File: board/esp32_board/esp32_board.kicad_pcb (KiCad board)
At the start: 2 copper layers, 3 parts, among them J1 Screw_Terminal_01x19, J2 Screw_Terminal_01x19, U1 ESP32-DevKitC

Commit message: feat: Updated board
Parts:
- added J3: Conn_01x19_Socket, Connector_PinSocket_2.54mm:PinSocket_1x19_P2.54mm_Vertical, F.Cu at (118.5, 74.5)
- added J4: Conn_01x19_Pin, Connector_PinSocket_2.54mm:PinSocket_1x19_P2.54mm_Vertical, F.Cu at (100.5, 74.5)
- added J5: Conn_01x19_Socket, Connector_PinSocket_2.54mm:PinSocket_1x19_P2.54mm_Vertical, F.Cu at (180.0, 74.5)
- added J6: Conn_01x19_Pin, Connector_PinSocket_2.54mm:PinSocket_1x19_P2.54mm_Vertical, F.Cu at (199.0, 74.5)
- moved J1 27.5 mm to (218.5, 74.5)
- moved J2 23.0 mm to (80.5, 74.5)

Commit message: feat: Updated board and presentation
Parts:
- moved J1 122.3 mm to (108.0, 22.0)
- moved J6 113.8 mm to (98.0, 22.0)
- moved J5 105.9 mm to (88.0, 22.0)
- moved U1 98.9 mm to (51.5, 22.0)
- moved J3 92.8 mm to (42.0, 22.0)
- moved J4 86.3 mm to (32.0, 22.0)
- moved J2 78.6 mm to (22.0, 22.0)
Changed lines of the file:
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@@
 	(footprint "PCM_Espressif:ESP32-DevKitC"
 		(layer "F.Cu")
-		(at 135.215 74.54812)
+		(at 51.5 21.96)
 		(descr "ESP32-DevKitC: https://docs.espressif.com/projects/esp-idf/en/latest/esp32/hw-reference/esp32/get-started-devkitc.html")
 		(tags "ESP32")
@@
 	(footprint "Connector_PinSocket_2.54mm:PinSocket_1x19_P2.54mm_Vertical"
 		(layer "F.Cu")
-		(at 180 74.5)
+		(at 88 22)
 		(descr "Through hole straight socket strip, 1x19, 2.54mm pitch, single row (from Kicad 4.0.7), script generated")
 		(tags "Through hole socket strip THT 1x19 2.54mm single row")
@@
 	(footprint "Connector_PinHeader_2.54mm:PinHeader_1x19_P2.54mm_Vertical"
 		(layer "F.Cu")
-		(at 218.5 74.5)
+		(at 108 22)
 		(descr "Through hole straight pin header, 1x19, 2.54mm pitch, single row")
 		(tags "Through hole pin header THT 1x19 2.54mm single row")
@@
 	(footprint "Connector_PinSocket_2.54mm:PinSocket_1x19_P2.54mm_Vertical"
 		(layer "F.Cu")
-		(at 100.5 74.5)
+		(at 32 22)
 		(descr "Through hole straight socket strip, 1x19, 2.54mm pitch, single row (from Kicad 4.0.7), script generated")
 		(tags "Through hole socket strip THT 1x19 2.54mm single row")
@@
 	(footprint "Connector_PinSocket_2.54mm:PinSocket_1x19_P2.54mm_Vertical"
 		(layer "F.Cu")
-		(at 118.5 74.5)
+		(at 42 22)
 		(descr "Through hole straight socket strip, 1x19, 2.54mm pitch, single row (from Kicad 4.0.7), script generated")
 		(tags "Through hole socket strip THT 1x19 2.54mm single row")
@@
 	(footprint "Connector_PinHeader_2.54mm:PinHeader_1x19_P2.54mm_Vertical"
 		(layer "F.Cu")
-		(at 80.5 74.5)
+		(at 22 22)
 		(descr "Through hole straight pin header, 1x19, 2.54mm pitch, single row")
 		(tags "Through hole pin header THT 1x19 2.54mm single row")
@@
 	(footprint "Connector_PinSocket_2.54mm:PinSocket_1x19_P2.54mm_Vertical"
 		(layer "F.Cu")
-		(at 199 74.5)
+		(at 98 22)
 		(descr "Through hole straight socket strip, 1x19, 2.54mm pitch, single row (from Kicad 4.0.7), script generated")
 		(tags "Through hole socket strip THT 1x19 2.54mm single row")

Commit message: feat: Updated docs and board
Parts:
- added compass1: ~, slon_modules:compass, F.Cu at (108.5, 85.4)
- added gps1: ~, slon_modules:gps, F.Cu at (175.5, 88.3)
- added relay1: ~, slon_modules:relay, F.Cu at (147.5, 66.4)
- added relay2: ~, slon_modules:relay, F.Cu at (144.0, 70.4)
- moved J1 108.9 mm to (191.0, 92.5)
- moved J2 108.9 mm to (105.0, 92.5)
- moved J3 108.9 mm to (125.0, 92.5)
- moved J4 108.9 mm to (115.0, 92.5)
- moved J5 108.9 mm to (171.0, 92.5)
- moved J6 108.9 mm to (181.0, 92.5)
- moved U1 108.9 mm to (134.5, 92.4)

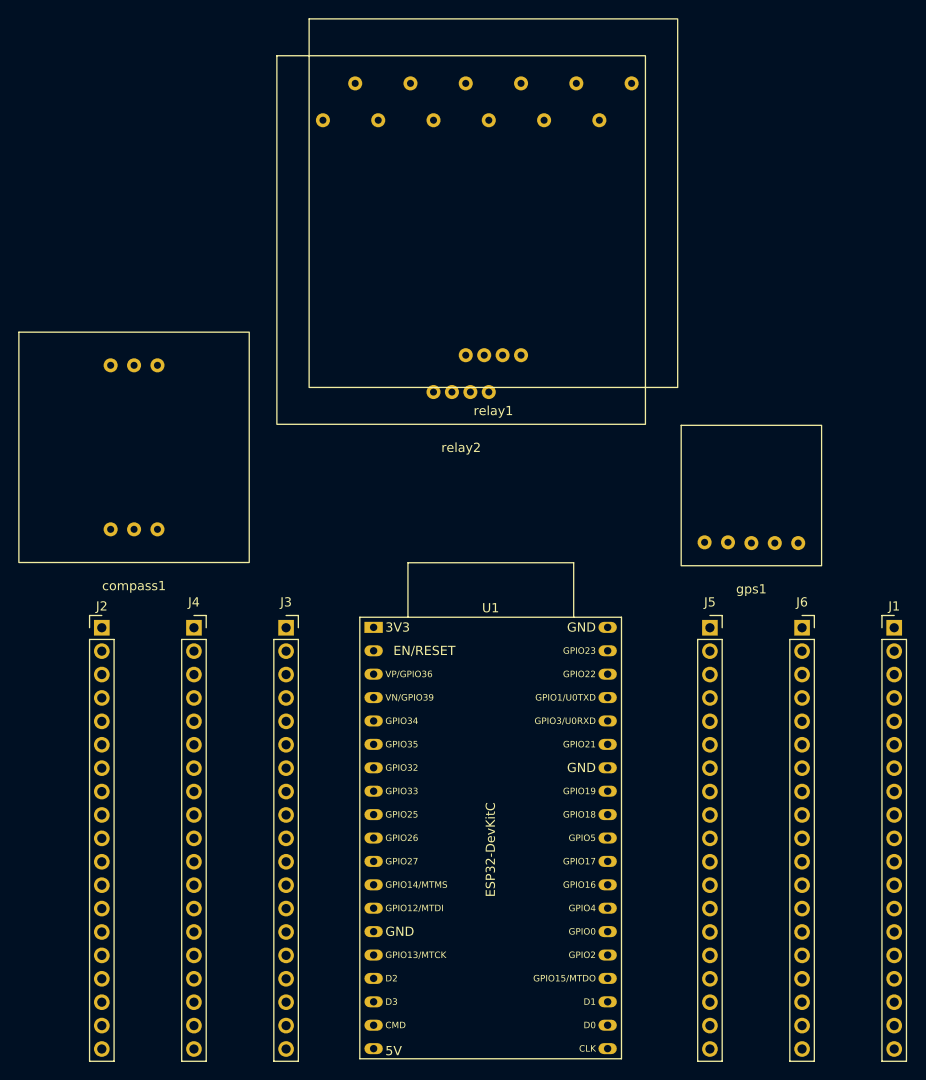
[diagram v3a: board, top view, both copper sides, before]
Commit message: feat(board): Added roads
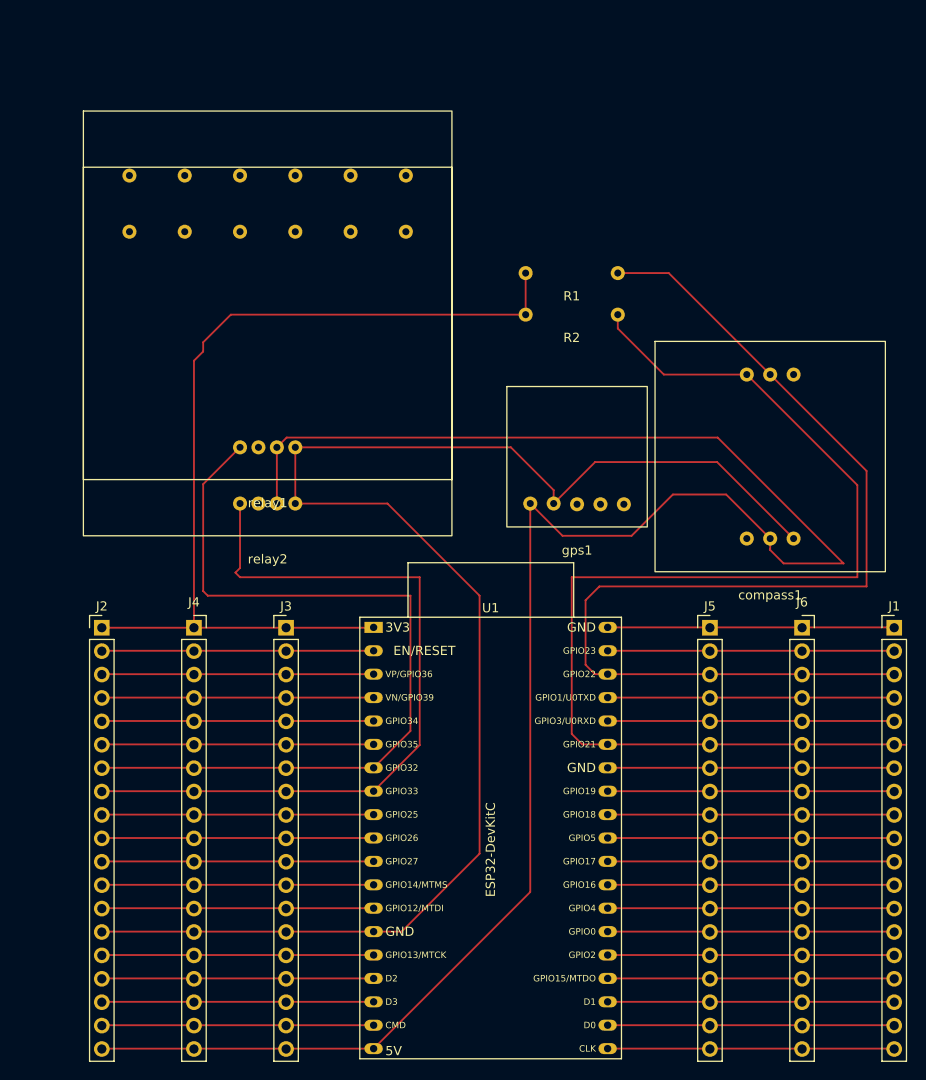
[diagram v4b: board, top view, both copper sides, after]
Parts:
- added R1: 2200, slon_modules:r, F.Cu at (156.0, 56.5)
- added R2: 2200, slon_modules:r, F.Cu at (156.0, 61.0)
- J3, J5: footprint Connector_PinSocket_2.54mm:PinSocket_1x19_P2.54mm_Vertical -> Connector_PinHeader_2.54mm:PinHeader_1x19_P2.54mm_Vertical
- moved compass1 69.0 mm to (177.5, 86.4)
- moved relay1 26.5 mm to (123.0, 76.4)
- moved relay2 24.2 mm to (123.0, 82.5)
- moved gps1 19.4 mm to (156.6, 84.1)
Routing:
- net GND: track 0.00 -> 227.8 mm
- net V5: track 0.00 -> 210.6 mm
- net 21: track 0.00 -> 129.4 mm
- net 22: track 0.00 -> 120.5 mm
- net 3V3: track 0.00 -> 101.7 mm
- net 32: track 0.00 -> 89.8 mm
- net 33: track 0.00 -> 82.7 mm
- net SD0: track 0.00 -> 31.1 mm
- net CLK: track 0.00 -> 31.1 mm
- net 15: track 0.00 -> 31.1 mm
- net RX: track 0.00 -> 31.1 mm
- net 5: track 0.00 -> 31.1 mm
- net 19: track 0.00 -> 31.1 mm
- net 16: track 0.00 -> 31.1 mm
- net 0: track 0.00 -> 31.1 mm
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
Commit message: feat(board): Updated board
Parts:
- moved relay1 0.10 mm to (123.0, 76.5)
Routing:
- net 16: track 31.1 -> 87.5 mm
- net V5: track 210.6 -> 158.0 mm
- net 17: track 31.1 -> 79.8 mm
- net GND: track 227.8 -> 214.2 mm
- net 3V3: track 101.7 -> 94.1 mm
- net 32: track 89.8 -> 85.7 mm
- net (no net): vias 0 -> 4
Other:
- board outline added: 95.5 x 106 mm

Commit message: feat(board): Updated board
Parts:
- removed relay1, relay2: ~, slon_modules:relay
- moved compass1 9.50 mm to (177.5, 76.9)
- moved gps1 3.50 mm to (153.1, 84.1)
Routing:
- net 32: track 85.7 -> 29.5 mm
- net 33: track 82.7 -> 29.5 mm
- net GND: track 214.2 -> 177.8 mm
- net V5: track 158.0 -> 179.3 mm
- net 3V3: track 94.1 -> 79.0 mm
- net 22: track 120.5 -> 134.7 mm
- net 21: track 129.4 -> 134.7 mm
- net 16: track 87.5 -> 91.4 mm
- net 17: track 79.8 -> 81.2 mm
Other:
- board size 95.5 x 106 mm -> 100 x 110 mm

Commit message: feat(board): Updated board
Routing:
- net 16: track 91.4 -> 86.8 mm
- net 17: track 81.2 -> 80.4 mm
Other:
- board size 100 x 110 mm -> 95.5 x 105 mm

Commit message: feat: Updated docs and board
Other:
- board size 95.5 x 105 mm -> 95.5 x 110 mm
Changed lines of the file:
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@@
 		(pad_to_mask_clearance 0)
 		(allow_soldermask_bridges_in_footprints no)
+		(grid_origin 100.25 35.5)
 		(pcbplotparams
-			(layerselection 0x00010fc_ffffffff)
+			(layerselection 0x0001000_7fffffff)
 			(plot_on_all_layers_selection 0x0000000_00000000)
 			(disableapertmacros no)
@@
 			(svgprecision 4)
 			(plotframeref no)
-			(viasonmask no)
+			(viasonmask yes)
 			(mode 1)
 			(useauxorigin no)
@@
 			(pdf_back_fp_property_popups yes)
 			(dxfpolygonmode yes)
-			(dxfimperialunits yes)
+			(dxfimperialunits no)
 			(dxfusepcbnewfont yes)
 			(psnegative no)
 			(psa4output no)
-			(plotreference yes)
-			(plotvalue yes)
-			(plotfptext yes)
+			(plotreference no)
+			(plotvalue no)
+			(plotfptext no)
 			(plotinvisibletext no)
 			(sketchpadsonfab no)
 			(subtractmaskfromsilk no)
-			(outputformat 1)
+			(outputformat 3)
 			(mirror no)
-			(drillshape 0)
+			(drillshape 2)
 			(scaleselection 1)
-			(outputdirectory "gbr/")
+			(outputdirectory "dxf/")
 		)
 	)
@@
 	)
 	(gr_rect
-		(start 100 38)
-		(end 195.5 143)
+		(start 100.25 35.5)
+		(end 195.75 145.5)
 		(stroke
 			(width 0.05)
